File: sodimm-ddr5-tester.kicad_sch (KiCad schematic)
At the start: 11 parts, among them M1001 Mech_Lightpipe_Mentor_1296.20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

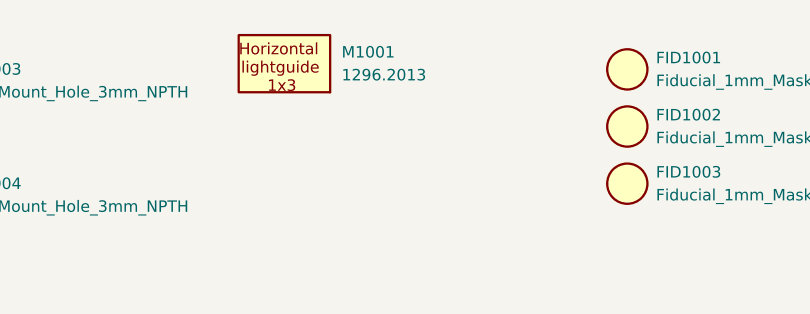
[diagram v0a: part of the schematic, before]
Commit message: Modify coolig fan circuit, replace radiator holes
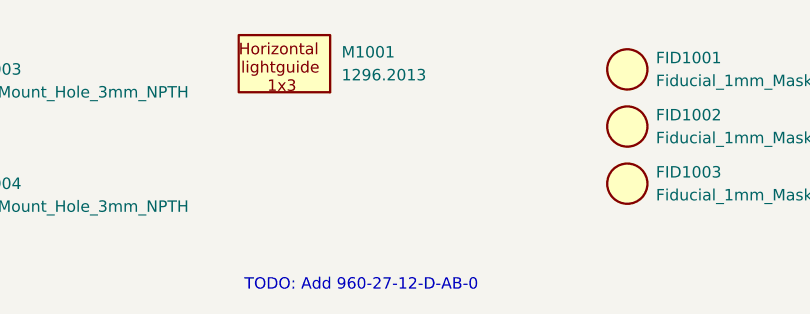
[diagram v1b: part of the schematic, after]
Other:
- note added: "TODO: Add 960-27-12-D-AB-0"
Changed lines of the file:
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@@
     )
+  )
+  (text "TODO: Add 960-27-12-D-AB-0" (at 166.37 290.195 0)
+    (effects (font (size 1.27 1.27)) (justify left bottom))
   )
   (text "LPDDR5 test board" (at 172.085 35.56 0)
@@
       (reference "#PWR012005") (unit 1) (value "GND") (footprint "")
     )
+    (path "/00000000-0000-0000-0000-000060225b0c/47b13192-a107-4ce6-bb5d-5fd0a47ca217"
+      (reference "#PWR?") (unit 1) (value "+5V") (footprint "")
+    )
+    (path "/00000000-0000-0000-0000-000060225b0c/8f9f0c69-0047-4e64-9cde-6c72079a626d"
+      (reference "#PWR?") (unit 1) (value "GND") (footprint "")
+    )
     (path "/00000000-0000-0000-0000-000060225b0c/00000000-0000-0000-0000-000062929c36"
       (reference "1V0") (unit 1) (value "TP_1mm_SMD") (footprint "data-center-rdimm-ddr4-tester-footprints:Testpoint_smd_1mm")
@@
       (reference "Q10002") (unit 1) (value "SI7613DN-T1-GE3") (footprint "antmicro-footprints:Vishay_PowerPAK_1212-8_Single")
     )
+    (path "/00000000-0000-0000-0000-000060225b0c/62668937-d3d7-4941-aeaf-e20d26397f5b"
+      (reference "Q?") (unit 1) (value "BSS138PW") (footprint "data-center-rdimm-ddr4-tester-footprints:SC70-3")
+    )
     (path "/00000000-0000-0000-0000-000060225b0c/229e8553-1652-4aab-b2d9-f6a357671f9c"
       (reference "R1001") (unit 1) (value "R_0R_22.4A_0603") (footprint "antmicro-footprints:R_0603_1608Metric")
@@
       (reference "R12003") (unit 1) (value "R_33R_0402") (footprint "data-center-rdimm-ddr4-tester-footprints:R_0402_1005Metric")
     )
+    (path "/00000000-0000-0000-0000-000060225b0c/635da235-874b-4788-b708-fed3d4b3b816"
+      (reference "R?") (unit 1) (value "R_10k_0402") (footprint "antmicro-footprints:R_0402_1005Metric")
+    )
     (path "/00000000-0000-0000-0000-000060225b0c/72b980fd-e4cb-4c6a-ac1f-b04708ae2ac5"

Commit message: Add loclib
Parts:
- FID1001, FID1002, FID1003, FID1004, FID1005, FID1006: footprint data-center-rdimm-ddr4-tester-footprints:Fiducial_1mm_Mask2mm -> sodimm-ddr5-tester-footprints:Fiducial_1mm_Mask2mm; symbol data-center-rdimm-ddr4-tester:Fiducial_1mm_Mask2mm -> sodimm-ddr5-tester:Fiducial_1mm_Mask2mm
- M1001: footprint data-center-rdimm-ddr4-tester-footprints:Mech_Lightpipe_Mentor_1296.2013 -> sodimm-ddr5-tester-footprints:Mech_Lightpipe_Mentor_1296.2013; symbol data-center-rdimm-ddr4-tester:Mech_Lightpipe_Mentor_1296.2013 -> sodimm-ddr5-tester:Mech_Lightpipe_Mentor_1296.2013
- MP1001, MP1002, MP1003, MP1004: footprint data-center-rdimm-ddr4-tester-footprints:mounting-hole-3mm-NPTH -> sodimm-ddr5-tester-footprints:mounting-hole-3mm-NPTH; symbol data-center-rdimm-ddr4-tester:PCB_Mount_Hole_3mm_NPTH -> sodimm-ddr5-tester:PCB_Mount_Hole_3mm_NPTH

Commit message: Update references of the components
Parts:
- removed MP1001, MP1002, MP1003, MP1004: PCB_Mount_Hole_3mm_NPTH, sodimm-ddr5-tester-footprints:mounting-hole-3mm-NPTH, symbol sodimm-ddr5-tester:PCB_Mount_Hole_3mm_NPTH
- added MP1001, MP1002, MP1003, MP1004, MP1005, MP1006: MP_NPTH_Drill3mm, sodimm-ddr5-tester-footprints:MP_NPTH_Drill3mm, symbol sodimm-ddr5-tester:MP_NPTH_Drill3mm
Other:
- moved on the sheet: M1001

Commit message: Bump revision to 1.0.0
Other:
- title: LPDDR5 Test Board -> SO-DIMM DDR5 Tester
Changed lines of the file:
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@@
   (paper "A3")
   (title_block
-    (title "LPDDR5 Test Board")
-    (date "2023-12-18")
-    (rev "0.0.99")
+    (title "SO-DIMM DDR5 Tester")
+    (date "2023-12")
+    (rev "1.0.0")
     (comment 1 "www.antmicro.com")
     (comment 2 "Antmicro Ltd")

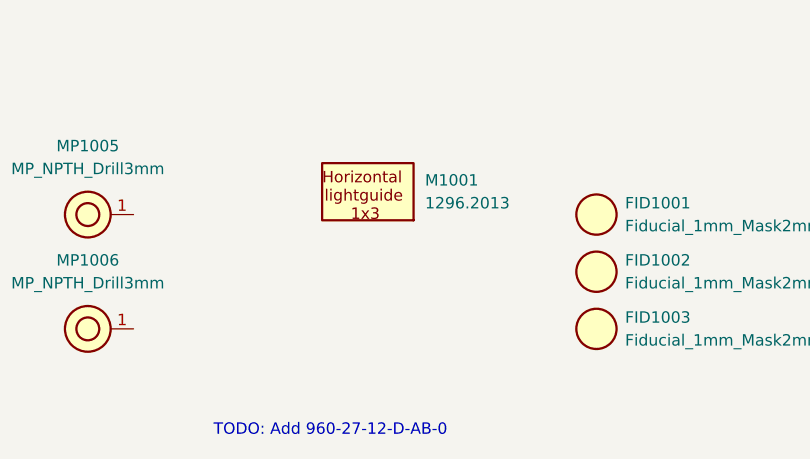
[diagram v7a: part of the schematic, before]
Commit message: Connect control and misc. signals, fix PCIe directions, rework I2C architecture, optimize DC-DC supply utilization
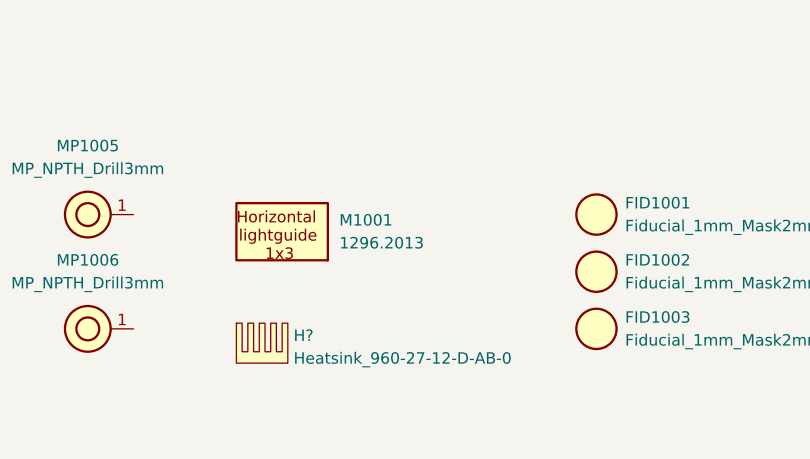
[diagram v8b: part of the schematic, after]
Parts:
- added H?: Heatsink_960-27-12-D-AB-0, antmicro-footprints:Heatsink_960-27-12-D-AB-0, symbol antmicroMechanicalParts:Heatsink_960-27-12-D-AB-0
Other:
- note removed: "TODO: Add 960-27-12-D-AB-0"
- moved on the sheet: M1001
